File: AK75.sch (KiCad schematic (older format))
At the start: 186 parts

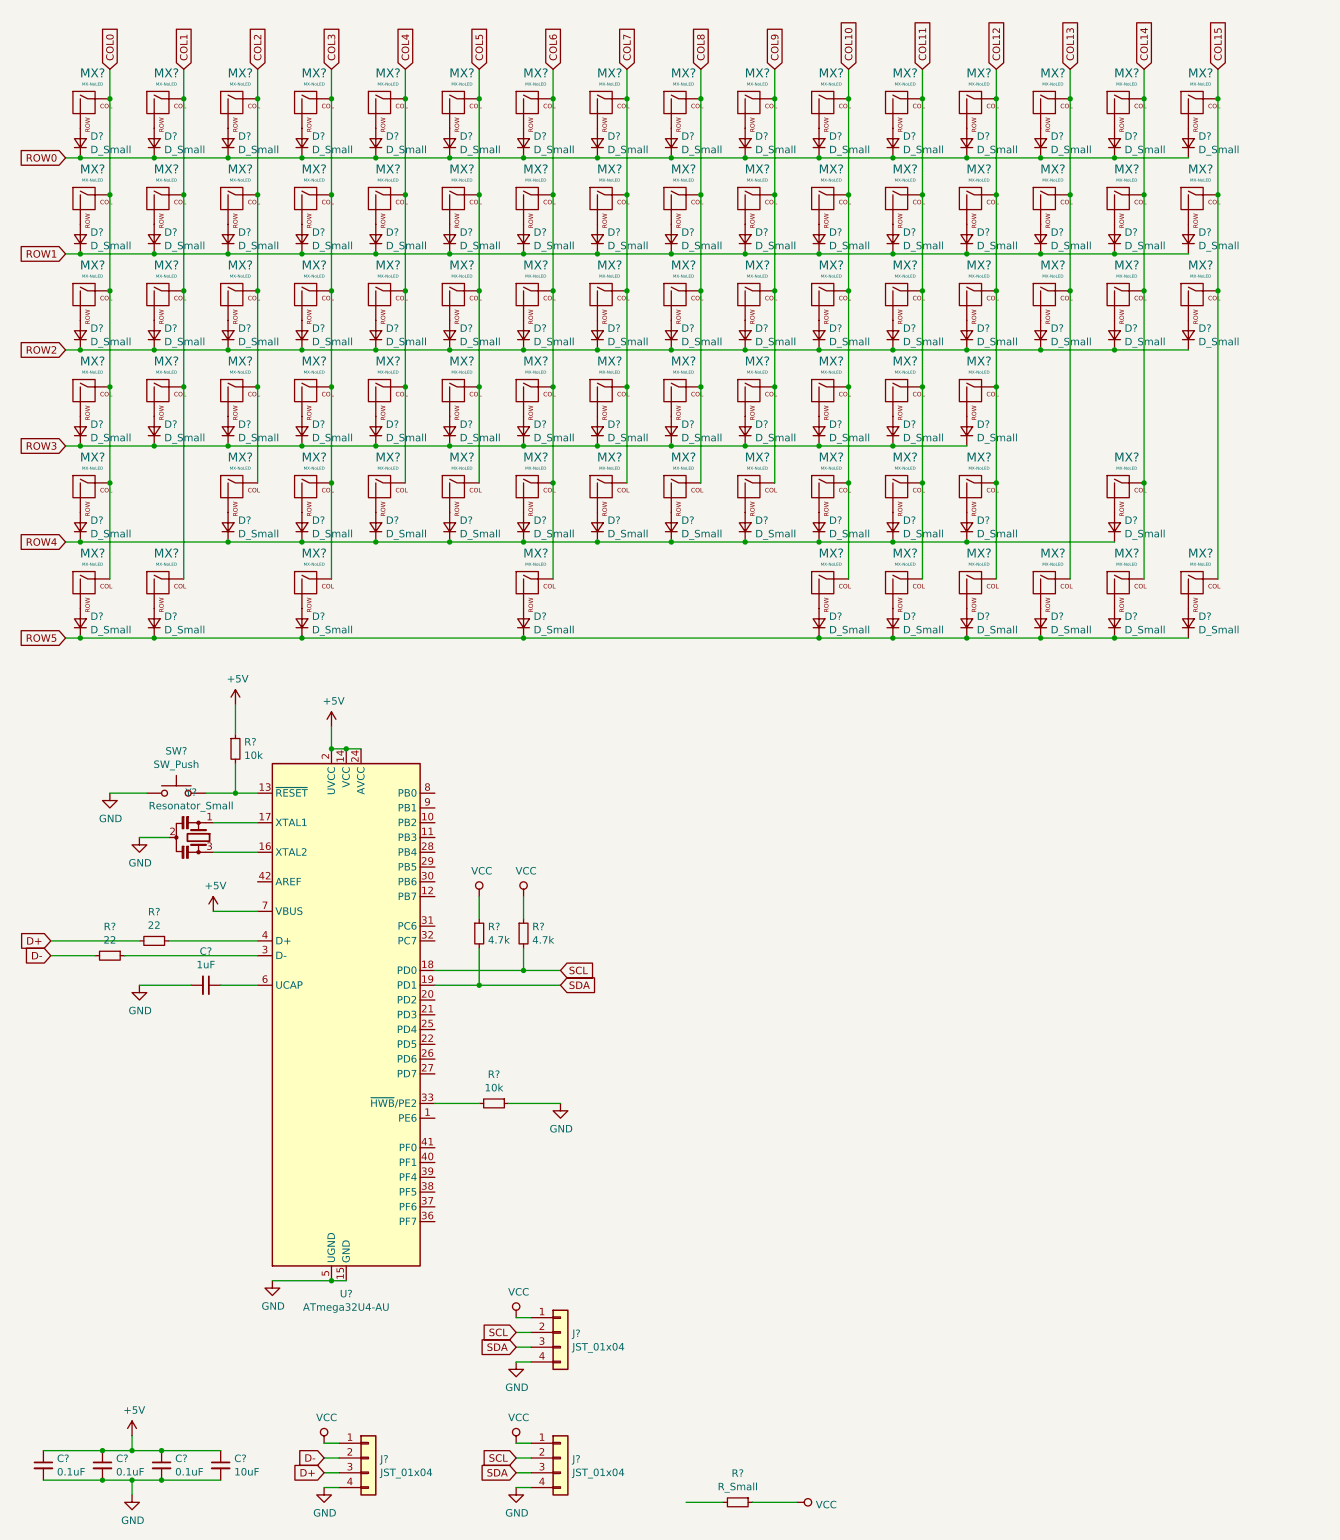
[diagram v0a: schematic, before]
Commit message: assigned footprints and added footprint for resonator
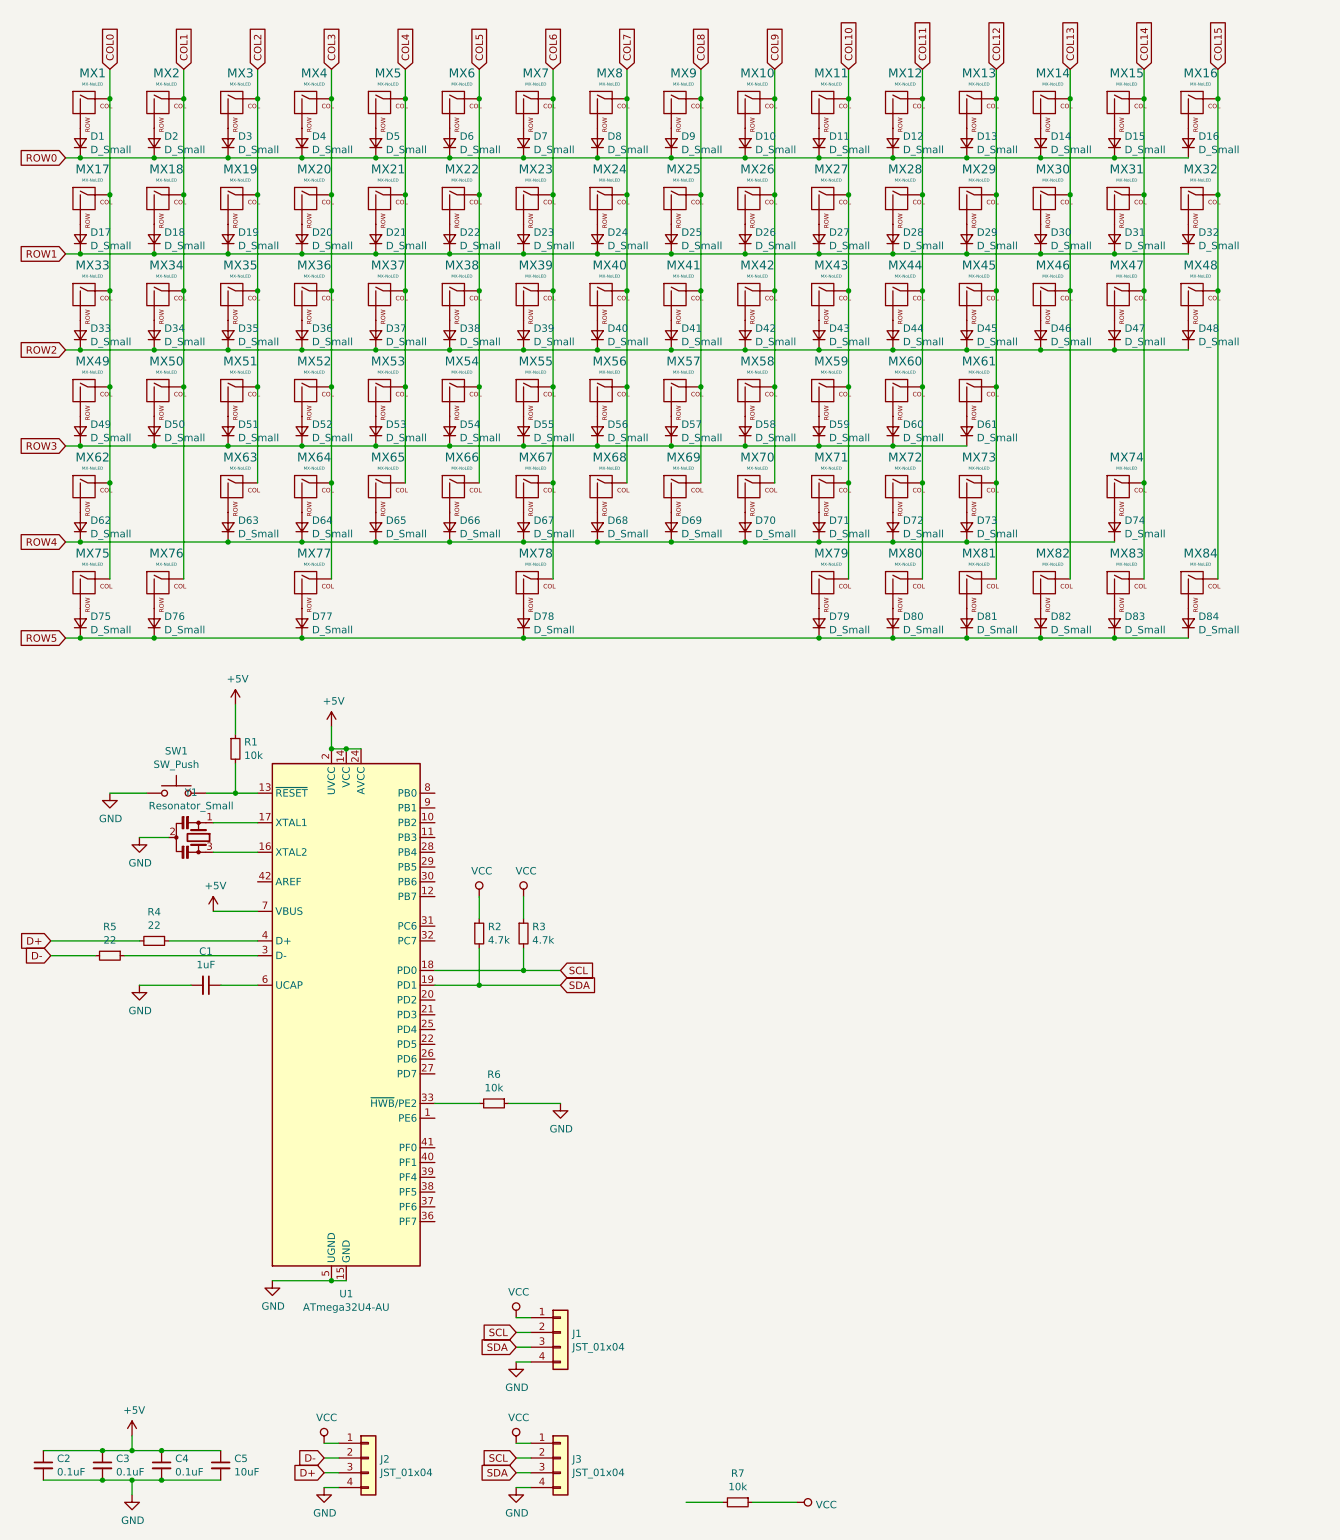
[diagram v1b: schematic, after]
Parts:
- C1, C2, C3, C4, C5: renamed from C?; footprint (none) -> Capacitor_SMD:C_0805_2012Metric
- D1, D10, D11, D12, D13, D14, D15, D16, D17, D18, D19, D2, D20, D21, D22, D23, D24, D25, D26, D27, D28, D29, D3, D30, D31, D32, D33, D34, D35, D36, D37, D38, D39, D4, D40, D41, D42, D43, D44, D45, D46, D47, D48, D49, D5, D50, D51, D52, D53, D54, D55, D56, D57, D58, D59, D6, D60, D61, D62, D63, D64, D65, D66, D67, D68, D69, D7, D70, D71, D72, D73, D74, D75, D76, D77, D78, D79, D8, D80, D81, D82, D83, D84, D9: renamed from D?; footprint (none) -> random-keyboard-parts:D_SOD-123-Pretty
- J1, J2, J3: renamed from J?; footprint (none) -> random-keyboard-parts:JST-SR-4
- R1, R2, R3, R4, R5, R6: renamed from R?; footprint (none) -> Resistor_SMD:R_0805_2012Metric
- R7: renamed from R?; value R_Small -> 10k; footprint (none) -> Resistor_SMD:R_0805_2012Metric
- SW1: renamed from SW?; footprint (none) -> random-keyboard-parts:SKQG-1155865
- gave numbers to parts that had none: 86

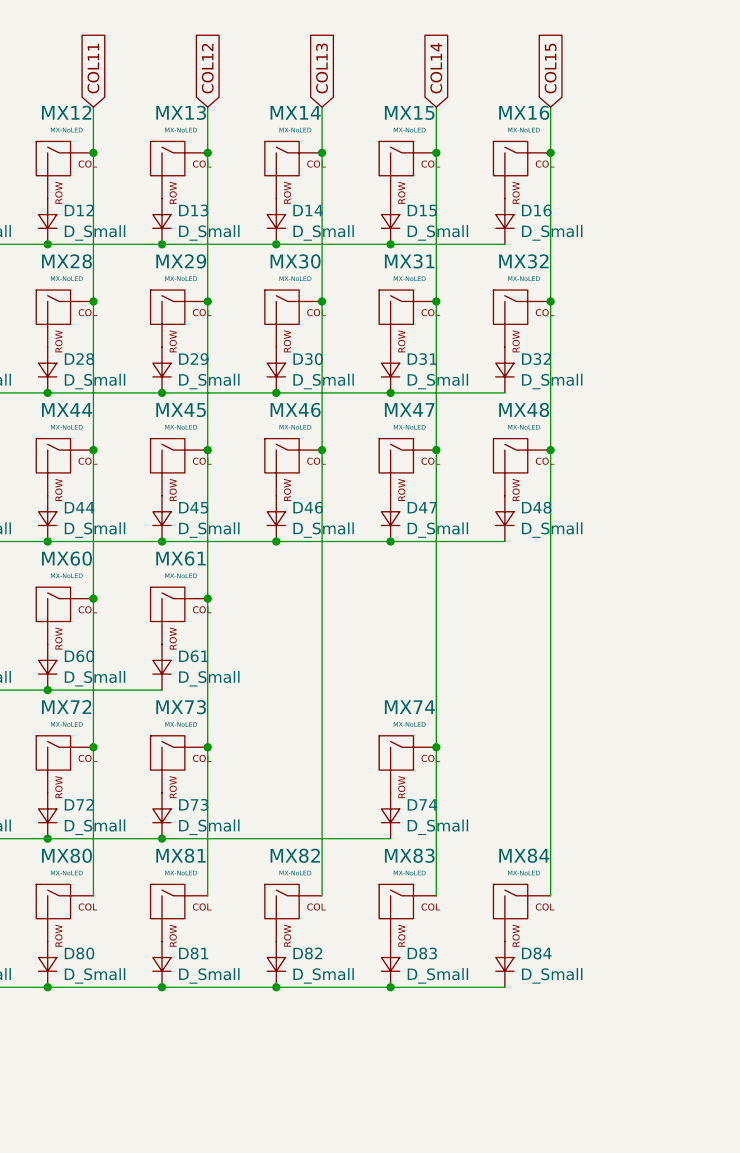
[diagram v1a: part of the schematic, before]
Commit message: updated switch matrix to TKL in sch
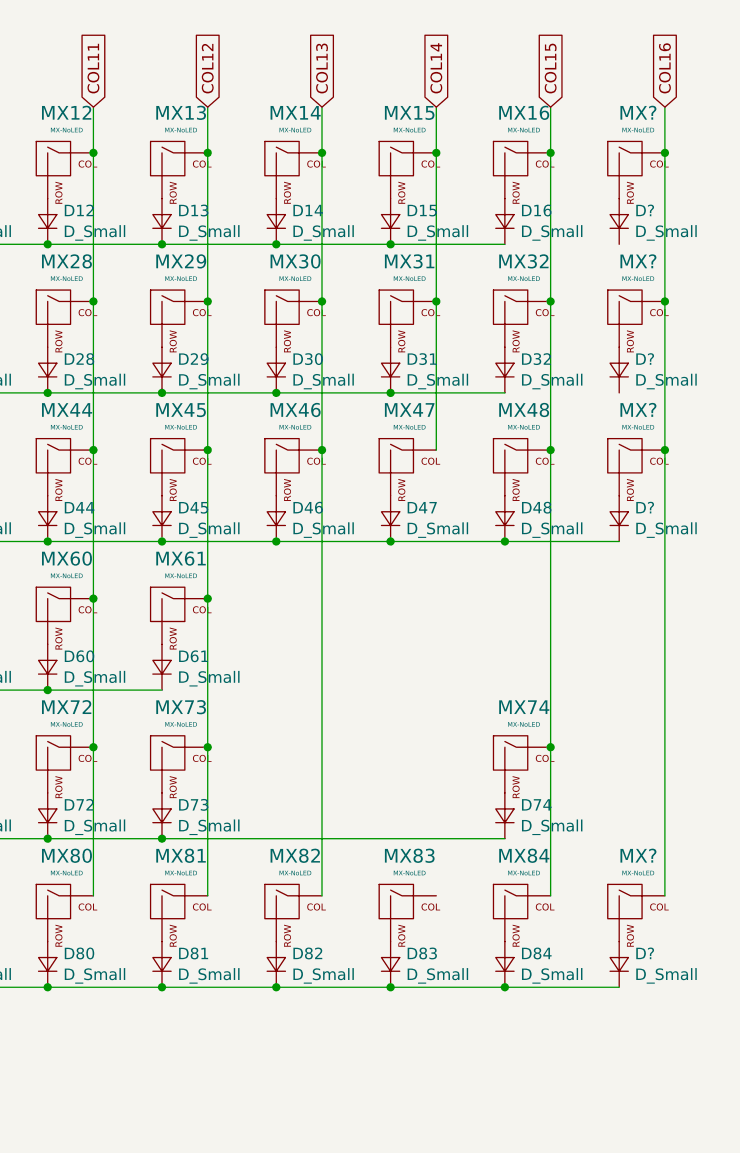
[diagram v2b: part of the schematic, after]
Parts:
- added D? (x3): D_Small, symbol Device:D_Small
- added D?: D_Small, random-keyboard-parts:D_SOD-123-Pretty, symbol Device:D_Small
- added MX? (x4): MX-NoLED, symbol MX_Alps_Hybrid:MX-NoLED
- Y1: footprint (none) -> DIMR_Keyboard_Parts:CSTCE
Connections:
- net COL14: no longer MX74.1 (COL), MX83.1 (COL)
- net COL15: now also MX74.1 (COL)
- net ROW2: now also D?.1 (K)
- net ROW5: now also D?.1 (K)
- new net: D?.2 (A), MX?.2 (ROW) (x4)
- new net COL16: MX?.1 (COL), MX?.1 (COL), MX?.1 (COL), MX?.1 (COL)
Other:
- moved on the sheet: D74, MX74
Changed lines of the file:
@@
 F 0 "Y1" V 1695 6150 50  0000 C CNN
 F 1 "Resonator_Small" V 1786 6150 50  0000 C CNN
-F 2 "" H 1975 6200 50  0001 C CNN
+F 2 "DIMR_Keyboard_Parts:CSTCE" H 1975 6200 50  0001 C CNN
 F 3 "~" H 1975 6200 50  0001 C CNN
 	1    2000 6200
@@
 L MX_Alps_Hybrid:MX-NoLED MX74
 U 1 1 5F0EB48E
-P 8250 3850
-F 0 "MX74" H 8283 4073 60  0000 C CNN
-F 1 "MX-NoLED" H 8283 3999 20  0000 C CNN
-F 2 "" H 7625 3825 60  0001 C CNN
-F 3 "" H 7625 3825 60  0001 C CNN
-	1    8250 3850
+P 8750 3850
+F 0 "MX74" H 8783 4073 60  0000 C CNN
+F 1 "MX-NoLED" H 8783 3999 20  0000 C CNN
+F 2 "" H 8125 3825 60  0001 C CNN
+F 3 "" H 8125 3825 60  0001 C CNN
+	1    8750 3850
 	1    0    0    -1
 $EndComp
@@
 L Device:D_Small D74
 U 1 1 5F0EB498
-P 8200 4100
-F 0 "D74" V 8246 4032 50  0000 R CNN
-F 1 "D_Small" V 8155 4032 50  0000 R CNN
-F 2 "random-keyboard-parts:D_SOD-123-Pretty" V 8200 4100 50  0001 C CNN
-F 3 "~" V 8200 4100 50  0001 C CNN
-	1    8200 4100
+P 8700 4100
+F 0 "D74" V 8746 4032 50  0000 R CNN
+F 1 "D_Small" V 8655 4032 50  0000 R CNN
+F 2 "random-keyboard-parts:D_SOD-123-Pretty" V 8700 4100 50  0001 C CNN
+F 3 "~" V 8700 4100 50  0001 C CNN
+	1    8700 4100
 	0    -1   -1   0
 $EndComp
@@
 Wire Wire Line
 	6700 4200 7200 4200
-Connection ~ 7200 4200
-Wire Wire Line
-	7200 4200 8200 4200
 Wire Wire Line
 	1100 4850 1200 4850
@@
 Wire Wire Line
 	8400 1850 8400 2500
-Connection ~ 8400 2500
-Wire Wire Line
-	8400 2500 8400 3800
-Connection ~ 8400 3800
-Wire Wire Line
-	8400 3800 8400 4450
 Wire Wire Line
 	8900 1000 8900 1200
@@
 Connection ~ 8900 2500
 Wire Wire Line
-	8900 2500 8900 4450
+	8900 2500 8900 3800
 Text GLabel 1400 1000 1    50   Input ~ 0
 COL0
@@
 Text GLabel 1100 4850 0    50   Input ~ 0
 ROW5
+$Comp
+L MX_Alps_Hybrid:MX-NoLED MX?
+U 1 1 5F29F827
+P 9250 1250
+F 0 "MX?" H 9283 1473 60  0000 C CNN
+F 1 "MX-NoLED" H 9283 1399 20  0000 C CNN
+F 2 "" H 8625 1225 60  0001 C CNN
+F 3 "" H 8625 1225 60  0001 C CNN
+	1    9250 1250
+	1    0    0    -1
+$EndComp
+$Comp
+L Device:D_Small D?
+U 1 1 5F2A248A
+P 9200 1500
+F 0 "D?" V 9246 1432 50  0000 R CNN
+F 1 "D_Small" V 9155 1432 50  0000 R CNN
+F 2 "" V 9200 1500 50  0001 C CNN
+F 3 "~" V 9200 1500 50  0001 C CNN
+	1    9200 1500
+	0    -1   -1   0
+$EndComp
+$Comp
+L MX_Alps_Hybrid:MX-NoLED MX?
+U 1 1 5F2A3C4A
+P 9250 1900
+F 0 "MX?" H 9283 2123 60  0000 C CNN
+F 1 "MX-NoLED" H 9283 2049 20  0000 C CNN
+F 2 "" H 8625 1875 60  0001 C CNN
+F 3 "" H 8625 1875 60  0001 C CNN
+	1    9250 1900
+	1    0    0    -1
+$EndComp
+$Comp
+L Device:D_Small D?
+U 1 1 5F2A3C54
+P 9200 2150
+F 0 "D?" V 9246 2082 50  0000 R CNN
+F 1 "D_Small" V 9155 2082 50  0000 R CNN
+F 2 "" V 9200 2150 50  0001 C CNN
+F 3 "~" V 9200 2150 50  0001 C CNN
+	1    9200 2150
+	0    -1   -1   0
+$EndComp
+$Comp
+L MX_Alps_Hybrid:MX-NoLED MX?
+U 1 1 5F2B1809
+P 9250 2550
+F 0 "MX?" H 9283 2773 60  0000 C CNN
+F 1 "MX-NoLED" H 9283 2699 20  0000 C CNN
+F 2 "" H 8625 2525 60  0001 C CNN
+F 3 "" H 8625 2525 60  0001 C CNN
+	1    9250 2550
+	1    0    0    -1
+$EndComp
+$Comp
+L Device:D_Small D?
+U 1 1 5F2B1813
+P 9200 2800
+F 0 "D?" V 9246 2732 50  0000 R CNN
+F 1 "D_Small" V 9155 2732 50  0000 R CNN
+F 2 "" V 9200 2800 50  0001 C CNN
+F 3 "~" V 9200 2800 50  0001 C CNN
+	1    9200 2800
+	0    -1   -1   0
+$EndComp
+$Comp
+L MX_Alps_Hybrid:MX-NoLED MX?
+U 1 1 5F2BED9E
+P 9250 4500
+F 0 "MX?" H 9283 4723 60  0000 C CNN
+F 1 "MX-NoLED" H 9283 4649 20  0000 C CNN
+F 2 "" H 8625 4475 60  0001 C CNN
+F 3 "" H 8625 4475 60  0001 C CNN
+	1    9250 4500
+	1    0    0    -1
+$EndComp
+$Comp
+L Device:D_Small D?
+U 1 1 5F2BEDA8
+P 9200 4750
+F 0 "D?" V 9246 4682 50  0000 R CNN
+F 1 "D_Small" V 9155 4682 50  0000 R CNN
+F 2 "random-keyboard-parts:D_SOD-123-Pretty" V 9200 4750 50  0001 C CNN
+F 3 "~" V 9200 4750 50  0001 C CNN
+	1    9200 4750
+	0    -1   -1   0
+$EndComp
+Wire Wire Line
+	8700 4850 9200 4850
+Wire Wire Line
+	9400 2500 9400 4450
+Connection ~ 8700 4850
+Connection ~ 8900 3800
+Wire Wire Line
+	8900 3800 8900 4450
+Wire Wire Line
+	8700 4200 7200 4200
+Connection ~ 7200 4200
+Wire Wire Line
+	9400 1000 9400 1200
+Connection ~ 9400 2500
+Connection ~ 9400 1200
+Wire Wire Line
+	9400 1200 9400 1850
+Connection ~ 9400 1850
+Wire Wire Line
+	9400 1850 9400 2500
+Wire Wire Line
+	9200 2900 8700 2900
+Connection ~ 8700 2900
+Text GLabel 9400 1000 1    50   Input ~ 0
+COL16
 $EndSCHEMATC
